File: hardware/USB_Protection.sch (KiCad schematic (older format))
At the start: 11 parts, among them Q1 DMN6140L, U12 TCPP01-M12, U301 USBLC6-2SC6

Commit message: added order references to parts
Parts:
- C1: Manufacturer KEMET -> Samsung Electro-Mechanics; Order https://www.mouser.at/ProductDetail/80-C0603C104M4R -> https://www.mouser.at/ProductDetail/Samsung-Electro-Mechani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
- C301: Manufacturer (none) -> KEMET; Order (none) -> https://www.mouser.at/ProductDetail/KEMET/C0603C103J5RACTU?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
- D1: Manufacturer (none) -> STMicroelectornics; Order (none) -> https://www.mouser.at/ProductDetail/STMicroelectronics/ESDA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
- D2: Manufacturer (none) -> ON Semiconductor; Order (none) -> https://www.mouser.at/ProductDetail/ON-Semiconductor/NSR20F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
- F301: Manufacturer (none) -> Littelfuse; Order (none) -> https://www.mouser.at/ProductDetail/Littelfuse/1812L050-60M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
- FB301: Manufacturer (none) -> Murata Electronics; Order (none) -> https://www.mouser.at/ProductDetail/Murata-Electronics/BLM1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
- R10, R11: Manufacturer (none) -> TE Connectivity / Holsworthy; Order (none) -> https://www.mouser.at/ProductDetail/TE-Connectivity-Holswor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
- U12: Manufacturer (none) -> STMicroelectornics; Order (none) -> https://www.mouser.at/ProductDetail/STMicroelectronics/TCPP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
- U301: Manufacturer (none) -> STMicroelectornics; Order (none) -> https://www.mouser.at/ProductDetail/STMicroelectronics/USBL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
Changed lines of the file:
@@
 F 2 "Package_DFN_QFN:QFN-12-1EP_3x3mm_P0.51mm_EP1.45x1.45mm" H 6200 4150 50  0001 C CNN
 F 3 "" H 6200 4150 50  0001 C CNN
+F 4 "STMicroelectornics" H 5000 3150 50  0001 C CNN "Manufacturer"
+F 5 "https://www.mouser.at/ProductDetail/STMicroelectronics/TCPP01-M12?qs=%252B6g0mu59x7KCafIwapwG2A%3D%3D" H 5000 3150 50  0001 C CNN "Order"
 	1    5000 3150
 	1    0    0    -1
@@
 F 2 "Diode_SMD:D_0603_1608Metric" V 2100 2400 50  0001 C CNN
 F 3 "~" V 2100 2400 50  0001 C CNN
+F 4 "STMicroelectornics" H 2100 2400 50  0001 C CNN "Manufacturer"
+F 5 "https://www.mouser.at/ProductDetail/STMicroelectronics/ESDA25P35-1U1M?qs=%2Fha2pyFadujUszDsZav4Fdl71EEjkmI2eQjtkMFuQaA97IC29zSS8w%3D%3D" H 2100 2400 50  0001 C CNN "Order"
 	1    2100 2400
 	0    1    1    0
@@
 F 2 "Resistor_SMD:R_0603_1608Metric" H 3000 2400 50  0001 C CNN
 F 3 "~" H 3000 2400 50  0001 C CNN
+F 4 "TE Connectivity / Holsworthy" H 3000 2400 50  0001 C CNN "Manufacturer"
+F 5 "https://www.mouser.at/ProductDetail/TE-Connectivity-Holsworthy/CRGP0603F10K?qs=sGAEpiMZZMtlubZbdhIBIOInyB5Ysv8smNyg8wE1EWk%3D" H 3000 2400 50  0001 C CNN "Order"
 	1    3000 2400
 	1    0    0    -1
@@
 F 2 "Resistor_SMD:R_0603_1608Metric" H 3000 2700 50  0001 C CNN
 F 3 "~" H 3000 2700 50  0001 C CNN
+F 4 "TE Connectivity / Holsworthy" H 3000 2700 50  0001 C CNN "Manufacturer"
+F 5 "https://www.mouser.at/ProductDetail/TE-Connectivity-Holsworthy/CRGP0603F2K7?qs=wUXugUrL1qwUN23XEDlhqg%3D%3D" H 3000 2700 50  0001 C CNN "Order"
 	1    3000 2700
 	1    0    0    -1
@@
 F 2 "Diode_SMD:D_0603_1608Metric" V 3650 2500 50  0001 C CNN
 F 3 "~" V 3650 2500 50  0001 C CNN
+F 4 "ON Semiconductor" H 3650 2500 50  0001 C CNN "Manufacturer"
+F 5 "https://www.mouser.at/ProductDetail/ON-Semiconductor/NSR20F30NXT5G?qs=%2Fha2pyFaduiT4QgHJMtCRYYTP822FXVVx%2F52TlFmV4oVU2Zly4FJHw%3D%3D" H 3650 2500 50  0001 C CNN "Order"
 	1    3650 2500
 	0    -1   -1   0
@@
 F 2 "Capacitor_SMD:C_0603_1608Metric" H 3650 2850 50  0001 C CNN
 F 3 "https://www.mouser.at/datasheet/2/212/KEM_C1002_X7R_SMD-1102033.pdf" H 3650 2850 50  0001 C CNN
-F 4 "KEMET" H 3650 2850 50  0001 C CNN "Manufacturer"
-F 5 "https://www.mouser.at/ProductDetail/80-C0603C104M4R" H 3650 2850 50  0001 C CNN "Order"
+F 4 "Samsung Electro-Mechanics" H 3650 2850 50  0001 C CNN "Manufacturer"
+F 5 "https://www.mouser.at/ProductDetail/Samsung-Electro-Mechanics/CL10B104JB8NNNC?qs=349EhDEZ59oLEw5wc1qvGw%3D%3D" H 3650 2850 50  0001 C CNN "Order"
 	1    3650 2850
 	1    0    0    -1
@@
 F 2 "Fuse:Fuse_1812_4532Metric" H 1000 2000 50  0001 L CNN
 F 3 "~" H 950 2200 50  0001 C CNN
+F 4 "Littelfuse" H 950 2200 50  0001 C CNN "Manufacturer"
+F 5 "https://www.mouser.at/ProductDetail/Littelfuse/1812L050-60MR?qs=lM4gFlnEeEOTL6GzziLnSw%3D%3D" H 950 2200 50  0001 C CNN "Order"
 	1    950  2200
 	0    -1   -1   0
@@
 F 2 "Package_TO_SOT_SMD:SOT-23-6" H 6650 2700 50  0001 C CNN
 F 3 "https://www.st.com/resource/en/datasheet/usblc6-2.pdf" H 6850 3550 50  0001 C CNN
+F 4 "STMicroelectornics" H 6650 3200 50  0001 C CNN "Manufacturer"
+F 5 "https://www.mouser.at/ProductDetail/STMicroelectronics/USBLC6-2SC6?qs=po45yt2pPpu%2FhNIlwQdTlg%3D%3D" H 6650 3200 50  0001 C CNN "Order"
 	1    6650 3200
 	1    0    0    -1
@@
 F 1 "600R@100MHz" V 1704 2200 50  0000 C CNN
 F 2 "Inductor_SMD:L_0603_1608Metric" V 1780 2200 50  0001 C CNN
-F 3 "MI0603J601R-10" H 1850 2200 50  0001 C CNN
+F 3 "~" H 1850 2200 50  0001 C CNN
+F 4 "Murata Electronics" H 1850 2200 50  0001 C CNN "Manufacturer"
+F 5 "https://www.mouser.at/ProductDetail/Murata-Electronics/BLM18SP601SH1D?qs=W%2FMpXkg%252BdQ5h2YDxhlPgmw%3D%3D" H 1850 2200 50  0001 C CNN "Order"
 	1    1850 2200
 	0    1    1    0
@@
 F 2 "Capacitor_SMD:C_0603_1608Metric" H 1350 2350 50  0001 C CNN
 F 3 "~" H 1350 2350 50  0001 C CNN
+F 4 "KEMET" H 1350 2350 50  0001 C CNN "Manufacturer"
+F 5 "https://www.mouser.at/ProductDetail/KEMET/C0603C103J5RACTU?qs=BimOss5pjlFJEfKhlb7g1g%3D%3D" H 1350 2350 50  0001 C CNN "Order"
 	1    1350 2350
 	1    0    0    -1

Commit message: modified bom
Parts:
- C1: MNR (none) -> CL10B104JB8NNNC
- C301: MNR (none) -> C0603C103J5RACTU
- D1: MNR (none) -> ESDA25P35-1U1M
- D2: MNR (none) -> NSR20F30NXT5G
- F301: MNR (none) -> 1812L050/60MR
- FB301: MNR (none) -> BLM18SP601SH1D
- Q1: MNR (none) -> DMN6140L-13
- R10: MNR (none) -> CRGP0603F10K
- R11: MNR (none) -> CRGP0603F2K7
- U12: MNR (none) -> TCPP01-M12
- U301: MNR (none) -> USBLC6-2SC6
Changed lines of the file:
@@
 F 4 "STMicroelectornics" H 5000 3150 50  0001 C CNN "Manufacturer"
 F 5 "https://www.mouser.at/ProductDetail/STMicroelectronics/TCPP01-M12?qs=%252B6g0mu59x7KCafIwapwG2A%3D%3D" H 5000 3150 50  0001 C CNN "Order"
+F 6 "TCPP01-M12" H 5000 3150 50  0001 C CNN "MNR"
 	1    5000 3150
 	1    0    0    -1
@@
 F 4 "STMicroelectornics" H 2100 2400 50  0001 C CNN "Manufacturer"
 F 5 "https://www.mouser.at/ProductDetail/STMicroelectronics/ESDA25P35-1U1M?qs=%2Fha2pyFadujUszDsZav4Fdl71EEjkmI2eQjtkMFuQaA97IC29zSS8w%3D%3D" H 2100 2400 50  0001 C CNN "Order"
+F 6 "ESDA25P35-1U1M" H 2100 2400 50  0001 C CNN "MNR"
 	1    2100 2400
 	0    1    1    0
@@
 F 4 "TE Connectivity / Holsworthy" H 3000 2400 50  0001 C CNN "Manufacturer"
 F 5 "https://www.mouser.at/ProductDetail/TE-Connectivity-Holsworthy/CRGP0603F10K?qs=sGAEpiMZZMtlubZbdhIBIOInyB5Ysv8smNyg8wE1EWk%3D" H 3000 2400 50  0001 C CNN "Order"
+F 6 "CRGP0603F10K" H 3000 2400 50  0001 C CNN "MNR"
 	1    3000 2400
 	1    0    0    -1
@@
 F 4 "TE Connectivity / Holsworthy" H 3000 2700 50  0001 C CNN "Manufacturer"
 F 5 "https://www.mouser.at/ProductDetail/TE-Connectivity-Holsworthy/CRGP0603F2K7?qs=wUXugUrL1qwUN23XEDlhqg%3D%3D" H 3000 2700 50  0001 C CNN "Order"
+F 6 "CRGP0603F2K7" H 3000 2700 50  0001 C CNN "MNR"
 	1    3000 2700
 	1    0    0    -1
@@
 F 4 "ON Semiconductor" H 3650 2500 50  0001 C CNN "Manufacturer"
 F 5 "https://www.mouser.at/ProductDetail/ON-Semiconductor/NSR20F30NXT5G?qs=%2Fha2pyFaduiT4QgHJMtCRYYTP822FXVVx%2F52TlFmV4oVU2Zly4FJHw%3D%3D" H 3650 2500 50  0001 C CNN "Order"
+F 6 "NSR20F30NXT5G" H 3650 2500 50  0001 C CNN "MNR"
 	1    3650 2500
 	0    -1   -1   0
@@
 F 4 "Samsung Electro-Mechanics" H 3650 2850 50  0001 C CNN "Manufacturer"
 F 5 "https://www.mouser.at/ProductDetail/Samsung-Electro-Mechanics/CL10B104JB8NNNC?qs=349EhDEZ59oLEw5wc1qvGw%3D%3D" H 3650 2850 50  0001 C CNN "Order"
+F 6 "CL10B104JB8NNNC" H 3650 2850 50  0001 C CNN "MNR"
 	1    3650 2850
 	1    0    0    -1
@@
 F 4 "Diodes Incorporated" H 5000 2300 50  0001 C CNN "Manufacturer"
 F 5 "https://www.mouser.at/ProductDetail/Diodes-Incorporated/DMN6140L-13?qs=M%2FOdCRO8QQ13uYA06Fe%2F0A%3D%3D" H 5000 2300 50  0001 C CNN "Order"
+F 6 "DMN6140L-13" H 5000 2300 50  0001 C CNN "MNR"
 	1    5000 2300
 	0    -1   -1   0
@@
 F 4 "Littelfuse" H 950 2200 50  0001 C CNN "Manufacturer"
 F 5 "https://www.mouser.at/ProductDetail/Littelfuse/1812L050-60MR?qs=lM4gFlnEeEOTL6GzziLnSw%3D%3D" H 950 2200 50  0001 C CNN "Order"
+F 6 "1812L050/60MR" H 950 2200 50  0001 C CNN "MNR"
 	1    950  2200
 	0    -1   -1   0
@@
 F 4 "STMicroelectornics" H 6650 3200 50  0001 C CNN "Manufacturer"
 F 5 "https://www.mouser.at/ProductDetail/STMicroelectronics/USBLC6-2SC6?qs=po45yt2pPpu%2FhNIlwQdTlg%3D%3D" H 6650 3200 50  0001 C CNN "Order"
+F 6 "USBLC6-2SC6" H 6650 3200 50  0001 C CNN "MNR"
 	1    6650 3200
 	1    0    0    -1
@@
 F 4 "Murata Electronics" H 1850 2200 50  0001 C CNN "Manufacturer"
 F 5 "https://www.mouser.at/ProductDetail/Murata-Electronics/BLM18SP601SH1D?qs=W%2FMpXkg%252BdQ5h2YDxhlPgmw%3D%3D" H 1850 2200 50  0001 C CNN "Order"
+F 6 "BLM18SP601SH1D" H 1850 2200 50  0001 C CNN "MNR"
 	1    1850 2200
 	0    1    1    0
@@
 F 4 "KEMET" H 1350 2350 50  0001 C CNN "Manufacturer"
 F 5 "https://www.mouser.at/ProductDetail/KEMET/C0603C103J5RACTU?qs=BimOss5pjlFJEfKhlb7g1g%3D%3D" H 1350 2350 50  0001 C CNN "Order"
+F 6 "C0603C103J5RACTU" H 1350 2350 50  0001 C CNN "MNR"
 	1    1350 2350
 	1    0    0    -1

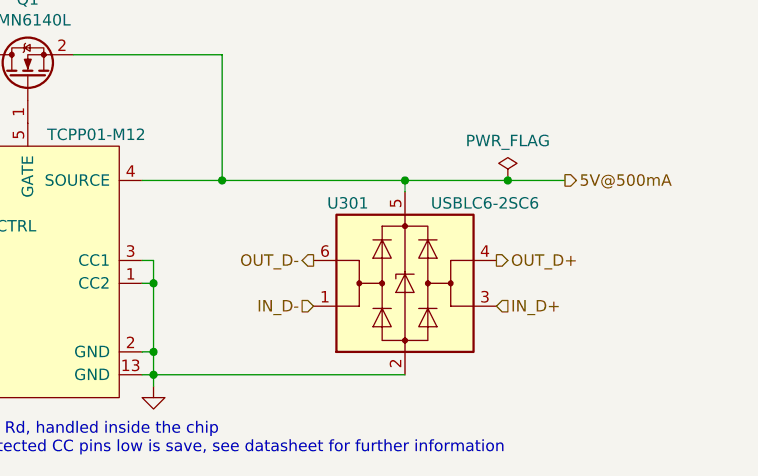
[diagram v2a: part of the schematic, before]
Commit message: Fixed two hardware issues.
Issue 1: Swapped USB D+/- lines
Issue 2: Wrong schematic smybol for power switch
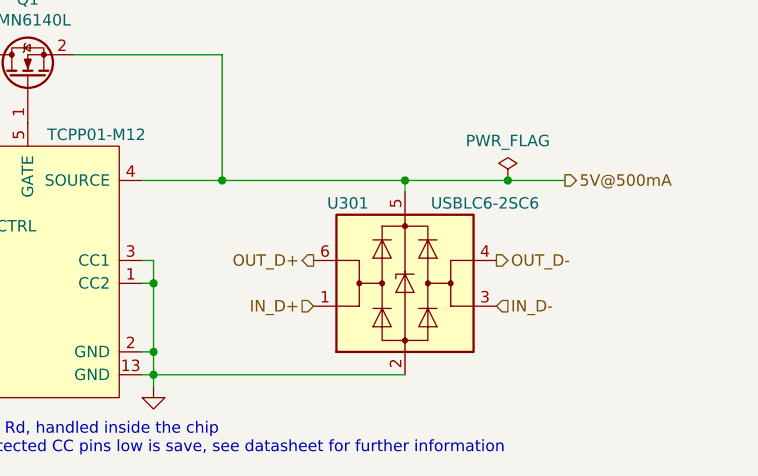
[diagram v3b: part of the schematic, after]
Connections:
- net IN_D+: now also U301.1 (I/O1); no longer U301.3 (I/O2)
- net IN_D-: now also U301.3 (I/O2); no longer U301.1 (I/O1)
- net OUT_D+: now also U301.6 (I/O1); no longer U301.4 (I/O2)
- net OUT_D-: now also U301.4 (I/O2); no longer U301.6 (I/O1)
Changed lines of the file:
@@
 Wire Wire Line
 	1350 2500 1350 2450
+Text HLabel 6250 3100 0    50   Output ~ 0
+OUT_D+
 Text HLabel 7050 3100 2    50   Output ~ 0
-OUT_D+
-Text HLabel 6250 3100 0    50   Output ~ 0
 OUT_D-
+Text HLabel 6250 3300 0    50   Input ~ 0
+IN_D+
 Text HLabel 7050 3300 2    50   Input ~ 0
-IN_D+
-Text HLabel 6250 3300 0    50   Input ~ 0
 IN_D-
 $Comp

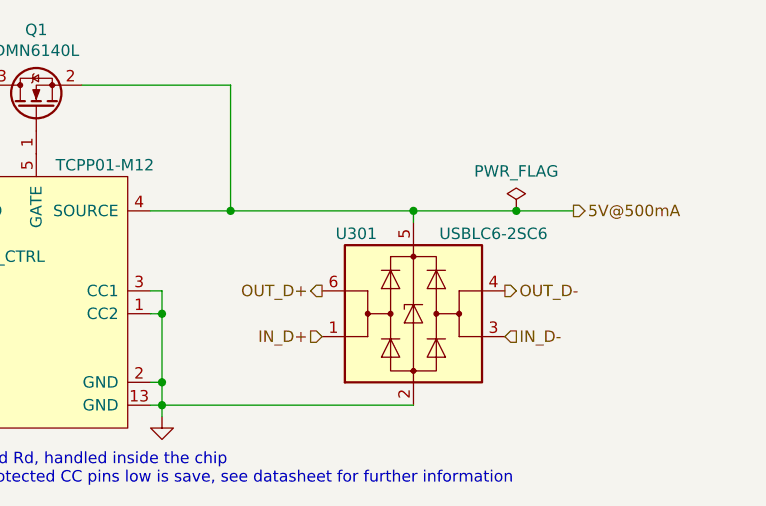
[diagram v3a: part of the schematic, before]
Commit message: New uC, ditched FTDI chip, and more!
Need to improve the schematic a little bit more.
For example, I want to be able to turn the LED Drivers off using
a MOSFET.

For the PCB Layout: I want to move as many components as possible
to the top layer, so that they are visible when in the case.
Also, I have to consider solderability of the components, the more
complex should all be on one layer for easier soldering.

Next up: Finishing the schematic, improving component placement,
and routing!
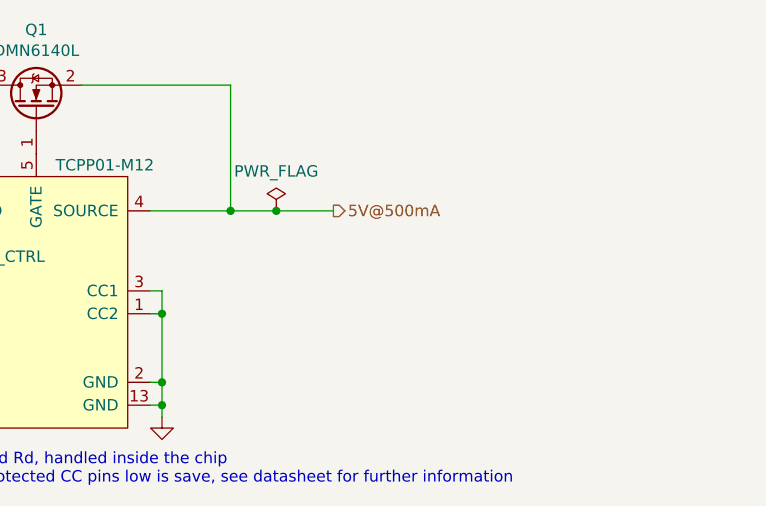
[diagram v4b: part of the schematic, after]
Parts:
- removed U301: USBLC6-2SC6, Package_TO_SOT_SMD:SOT-23-6, symbol Power_Protection:USBLC6-2SC6
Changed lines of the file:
@@
 $Descr A4 11693 8268
 encoding utf-8
-Sheet 3 7
+Sheet 3 6
 Title "aWristWatch"
 Date "2021-04-05"
@@
 	0    -1   -1   0
 $EndComp
-Text HLabel 7350 2750 2    50   Output ~ 0
+Text HLabel 6300 2750 2    50   Output ~ 0
 5V@500mA
 Wire Wire Line
@@
 	3000 2200 2100 2200
 Connection ~ 3000 2200
-Connection ~ 5850 2750
 Wire Wire Line
 	5500 2750 5850 2750
@@
 Wire Wire Line
 	5200 2200 5850 2200
-$Comp
-L Power_Protection:USBLC6-2SC6 U301
-U 1 1 605F9EDA
-P 6650 3200
-F 0 "U301" H 6400 3550 50  0000 C CNN
-F 1 "USBLC6-2SC6" H 7000 3550 50  0000 C CNN
-F 2 "Package_TO_SOT_SMD:SOT-23-6" H 6650 2700 50  0001 C CNN
-F 3 "https://www.st.com/resource/en/datasheet/usblc6-2.pdf" H 6850 3550 50  0001 C CNN
-F 4 "STMicroelectornics" H 6650 3200 50  0001 C CNN "Manufacturer"
-F 5 "https://www.mouser.at/ProductDetail/STMicroelectronics/USBLC6-2SC6?qs=po45yt2pPpu%2FhNIlwQdTlg%3D%3D" H 6650 3200 50  0001 C CNN "Order"
-F 6 "USBLC6-2SC6" H 6650 3200 50  0001 C CNN "MNR"
-	1    6650 3200
-	1    0    0    -1
-$EndComp
-Wire Wire Line
-	7350 2750 7100 2750
-Wire Wire Line
-	6650 2750 6650 2800
-Wire Wire Line
-	5850 2750 6650 2750
-Connection ~ 6650 2750
-Wire Wire Line
-	5550 3600 6650 3600
 $Comp
 L Device:Ferrite_Bead_Small FB301
@@
 Wire Wire Line
 	1350 2500 1350 2450
-Text HLabel 6250 3100 0    50   Output ~ 0
-OUT_D+
-Text HLabel 7050 3100 2    50   Output ~ 0
-OUT_D-
-Text HLabel 6250 3300 0    50   Input ~ 0
-IN_D+
-Text HLabel 7050 3300 2    50   Input ~ 0
-IN_D-
 $Comp
 L power:PWR_FLAG #FLG0102
 U 1 1 606A9573
-P 7100 2750
-F 0 "#FLG0102" H 7100 2825 50  0001 C CNN
-F 1 "PWR_FLAG" H 7100 2923 50  0000 C CNN
-F 2 "" H 7100 2750 50  0001 C CNN
-F 3 "~" H 7100 2750 50  0001 C CNN
-	1    7100 2750
-	1    0    0    -1
-$EndComp
-Connection ~ 7100 2750
-Wire Wire Line
-	7100 2750 6650 2750
+P 6050 2750
+F 0 "#FLG0102" H 6050 2825 50  0001 C CNN
+F 1 "PWR_FLAG" H 6050 2923 50  0000 C CNN
+F 2 "" H 6050 2750 50  0001 C CNN
+F 3 "~" H 6050 2750 50  0001 C CNN
+	1    6050 2750
+	1    0    0    -1
+$EndComp
 Text Notes 3350 3250 0    50   ~ 0
 C1: 50V X7R
+Wire Wire Line
+	5850 2750 6050 2750
+Connection ~ 5850 2750
+Connection ~ 6050 2750
+Wire Wire Line
+	6050 2750 6300 2750
 $EndSCHEMATC
